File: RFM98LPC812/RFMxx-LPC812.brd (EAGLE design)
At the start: 60 x 38.7 mm, 33 parts, among them X1 BU-SMA-V, X2 BU-SMA-V

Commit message: getting close to done
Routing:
- net N$14: track 19.0 -> 6.93 mm
- net GND: track 214.8 -> 225.6 mm, vias 2 -> 3
- net VCC: track 119.8 -> 113.9 mm
- net N$45: track 0.00 -> 3.30 mm
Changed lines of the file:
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@@
 <description language="de">&lt;b&gt;EAGLE Design Rules&lt;/b&gt;
 &lt;p&gt;
-Die Standard-Design-Rules sind so gewÃ¤hlt, dass sie fÃ¼r
+Die Standard-Design-Rules sind so gewÃÂ¤hlt, dass sie fÃÂ¼r
 die meisten Anwendungen passen. Sollte ihre Platine
 besondere Anforderungen haben, treffen Sie die erforderlichen
@@
 <contactref element="C2" pad="1"/>
 <contactref element="JP8" pad="1"/>
-<wire x1="18.5166" y1="26.5176" x2="20.8026" y2="26.5176" width="0.254" layer="1"/>
-<wire x1="20.8026" y1="26.5176" x2="20.955" y2="26.455" width="0.254" layer="1"/>
-<wire x1="18.5166" y1="26.5176" x2="18.3642" y2="26.67" width="0.254" layer="1"/>
 <wire x1="39.0906" y1="12.7508" x2="39.140371875" y2="12.584065625" width="0.254" layer="16"/>
 <wire x1="10.795" y1="36.195" x2="10.795" y2="37.7825" width="0.4064" layer="1"/>
@@
 <wire x1="56.9214" y1="35.2044" x2="56.99" y2="35.21" width="0.254" layer="1"/>
 <wire x1="56.9214" y1="35.2044" x2="56.8325" y2="35.2425" width="0.254" layer="1"/>
-<wire x1="10.795" y1="36.195" x2="10.795" y2="26.67" width="0.4064" layer="1"/>
-<wire x1="10.795" y1="26.67" x2="16.9164" y2="26.67" width="0.4064" layer="1"/>
-<wire x1="16.9164" y1="26.67" x2="18.288" y2="26.67" width="0.4064" layer="1"/>
-<wire x1="18.288" y1="26.67" x2="18.3642" y2="26.67" width="0.4064" layer="1"/>
-<wire x1="18.3642" y1="26.67" x2="18.415" y2="26.67" width="0.4064" layer="1"/>
-<wire x1="18.288" y1="26.7462" x2="18.3642" y2="26.67" width="0.254" layer="1"/>
-<wire x1="18.288" y1="26.7462" x2="18.288" y2="26.67" width="0.254" layer="1"/>
-<wire x1="16.9164" y1="21.0312" x2="16.9164" y2="26.67" width="0.254" layer="1"/>
 <wire x1="52.578" y1="15.9512" x2="52.705" y2="15.875" width="0.254" layer="1"/>
 <wire x1="48.4632" y1="10.4648" x2="48.006" y2="10.4648" width="0.254" layer="1"/>
@@
 <wire x1="48.006" y1="10.4648" x2="47.85" y2="10.255" width="0.254" layer="1"/>
 <wire x1="52.578" y1="15.7226" x2="52.705" y2="15.875" width="0.254" layer="1"/>
-<wire x1="18.3642" y1="8.89" x2="16.9164" y2="21.0312" width="0" layer="19" extent="1-1"/>
+<wire x1="18.3642" y1="26.67" x2="20.955" y2="26.455" width="0" layer="19" extent="1-1"/>
+<wire x1="10.795" y1="36.195" x2="18.3642" y2="26.67" width="0" layer="19" extent="1-1"/>
+<wire x1="24.765" y1="9.525" x2="20.955" y2="26.455" width="0" layer="19" extent="1-16"/>
+<wire x1="10.795" y1="36.195" x2="10.795" y2="26.67" width="0.4064" layer="1"/>
+<wire x1="20.955" y1="26.67" x2="18.415" y2="26.67" width="0.6096" layer="1"/>
+<wire x1="10.795" y1="26.67" x2="18.415" y2="26.67" width="0.4064" layer="1"/>
 </signal>
 <signal name="N$6">
@@
 <wire x1="24.4602" y1="23.3172" x2="24.003" y2="22.86" width="0.254" layer="1"/>
 <wire x1="24.4602" y1="23.3172" x2="24.61" y2="23.495" width="0.254" layer="1"/>
-<wire x1="24.6888" y1="23.3172" x2="36.8046" y2="23.3172" width="0.254" layer="1"/>
+<wire x1="24.6888" y1="23.3172" x2="36.8046" y2="23.3172" width="0" layer="19" extent="1-16"/>
 <wire x1="36.8046" y1="23.3172" x2="36.99" y2="23.21" width="0.254" layer="1"/>
 <wire x1="24.6888" y1="23.3172" x2="24.61" y2="23.495" width="0.254" layer="1"/>
@@
 <contactref element="C2" pad="2"/>
 <contactref element="U$1" pad="16"/>
-<wire x1="18.5166" y1="28.1178" x2="20.8026" y2="28.1178" width="0.254" layer="1"/>
+<wire x1="18.5166" y1="28.1178" x2="20.8026" y2="28.1178" width="0.6096" layer="1"/>
 <wire x1="20.8026" y1="28.1178" x2="20.955" y2="28.155" width="0.254" layer="1"/>
 <wire x1="18.5166" y1="28.1178" x2="18.3642" y2="27.94" width="0.254" layer="1"/>
 <wire x1="18.288" y1="27.8892" x2="18.3642" y2="27.94" width="0.254" layer="1"/>
 <contactref element="R1" pad="1"/>
-<wire x1="33.8328" y1="30.6324" x2="33.6674" y2="30.4701" width="0.254" layer="16"/>
-<wire x1="33.8328" y1="35.433" x2="33.6674" y2="35.5699" width="0.254" layer="16"/>
 <wire x1="58.0644" y1="8.4074" x2="58.0644" y2="10.6934" width="0.254" layer="1"/>
 <wire x1="57.3786" y1="7.7216" x2="58.0644" y2="8.4074" width="0.254" layer="1"/>
@@
 <wire x1="1.8288" y1="36.1188" x2="1.69" y2="36.195" width="0.254" layer="1"/>
 <via x="6.6294" y="34.9758" extent="1-16" drill="0.6096"/>
+<wire x1="13.335" y1="20.955" x2="16.6878" y2="20.955" width="0" layer="19" extent="1-16"/>
 <wire x1="13.335" y1="20.955" x2="20.955" y2="20.955" width="0.4064" layer="16"/>
 <wire x1="20.955" y1="20.955" x2="20.955" y2="22.225" width="0.254" layer="16"/>
@@
 <wire x1="55.245" y1="7.62" x2="57.15" y2="7.62" width="0.4064" layer="16"/>
 <wire x1="57.15" y1="7.62" x2="57.15" y2="2.54" width="0.4064" layer="16"/>
-<wire x1="57.15" y1="2.54" x2="50.165" y2="2.54" width="0.4064" layer="16"/>
-<wire x1="50.165" y1="2.54" x2="50.165" y2="1.27" width="0.4064" layer="16"/>
-<wire x1="50.165" y1="1.27" x2="15.24" y2="1.27" width="0.4064" layer="16"/>
+<wire x1="57.15" y1="2.54" x2="52.1208" y2="2.54" width="0.4064" layer="16"/>
+<wire x1="52.1208" y1="2.54" x2="52.07" y2="2.54" width="0.4064" layer="16"/>
+<wire x1="52.07" y1="2.54" x2="52.07" y2="1.27" width="0.4064" layer="16"/>
+<wire x1="52.07" y1="1.27" x2="15.24" y2="1.27" width="0.4064" layer="16"/>
 <wire x1="15.24" y1="1.27" x2="1.905" y2="1.27" width="0.4064" layer="16"/>
 <wire x1="1.905" y1="2.54" x2="1.905" y2="3.175" width="0.4064" layer="16"/>
@@
 <contactref element="R4" pad="2"/>
 <wire x1="15.24" y1="1.27" x2="15.24" y2="10.16" width="0.4064" layer="16"/>
-<wire x1="34.29" y1="31.0896" x2="33.8328" y2="35.433" width="0" layer="19" extent="1-16"/>
-<wire x1="28.36" y1="21.9075" x2="26.67" y2="22.225" width="0" layer="19" extent="1-16"/>
-<wire x1="15.24" y1="10.16" x2="13.335" y2="20.955" width="0" layer="19" extent="16-16"/>
-<wire x1="57.1599" y1="2.5301" x2="57.15" y2="2.54" width="0" layer="19" extent="16-16"/>
-<wire x1="57.1599" y1="7.6299" x2="57.15" y2="7.62" width="0" layer="19" extent="16-16"/>
-<wire x1="4.445" y1="1.69" x2="4.3434" y2="1.778" width="0" layer="19" extent="1-1"/>
+<wire x1="33.8328" y1="30.6324" x2="33.8328" y2="35.433" width="0.254" layer="16"/>
+<wire x1="33.8328" y1="35.433" x2="33.6674" y2="35.5699" width="0.254" layer="16"/>
+<wire x1="33.8328" y1="30.6324" x2="33.6674" y2="30.4701" width="0.254" layer="16"/>
+<wire x1="4.3434" y1="1.8288" x2="4.445" y2="1.69" width="0.254" layer="1"/>
+<wire x1="4.3434" y1="1.8288" x2="4.3434" y2="1.778" width="0.254" layer="1"/>
+<wire x1="52.1208" y1="2.5146" x2="52.1208" y2="2.54" width="0.254" layer="16"/>
+<wire x1="52.1208" y1="2.5146" x2="52.0601" y2="2.5301" width="0.254" layer="16"/>
+<wire x1="16.6878" y1="11.6586" x2="16.6878" y2="20.955" width="0" layer="19" extent="1-16"/>
+<wire x1="15.3162" y1="10.287" x2="16.6878" y2="11.6586" width="0" layer="19" extent="1-16"/>
+<wire x1="15.3162" y1="10.287" x2="15.24" y2="10.16" width="0.254" layer="16"/>
+<wire x1="57.15" y1="7.7724" x2="57.1599" y2="7.6299" width="0.254" layer="16"/>
+<wire x1="57.15" y1="7.7724" x2="57.15" y2="7.62" width="0.254" layer="16"/>
+<wire x1="28.36" y1="21.9075" x2="26.67" y2="21.9075" width="0.4064" layer="1"/>
+<wire x1="26.67" y1="21.9075" x2="26.67" y2="22.225" width="0.4064" layer="1"/>
+<wire x1="26.67" y1="22.225" x2="26.67" y2="22.225" width="0" layer="19" extent="1-16"/>
+<via x="15.24" y="10.16" extent="1-16" drill="0.6"/>
+<wire x1="15.24" y1="10.16" x2="18.415" y2="10.16" width="0.4064" layer="1"/>
 </signal>
 <signal name="N$11">
@@
 <contactref element="C1" pad="2"/>
 <contactref element="U$5" pad="16"/>
-<wire x1="18.3642" y1="10.16" x2="21.59" y2="10.375" width="0" layer="19" extent="1-1"/>
+<wire x1="18.5166" y1="10.287" x2="21.4884" y2="10.287" width="0.6096" layer="1"/>
+<wire x1="21.4884" y1="10.287" x2="21.59" y2="10.375" width="0.254" layer="1"/>
+<wire x1="18.5166" y1="10.287" x2="18.3642" y2="10.16" width="0.254" layer="1"/>
 </signal>
 </signals>

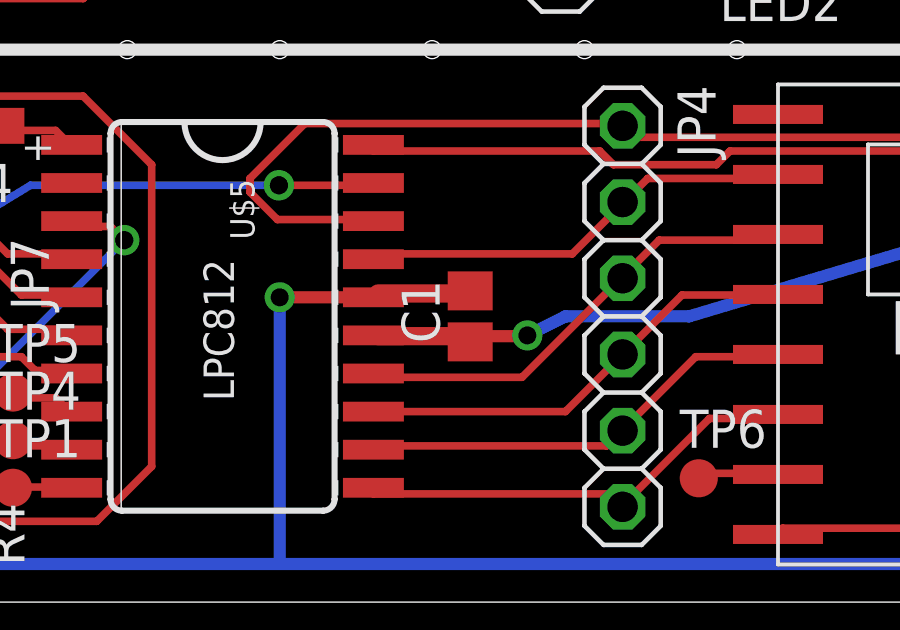
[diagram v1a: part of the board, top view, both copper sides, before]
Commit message: fixed inconsistency by hand editing .brd XML
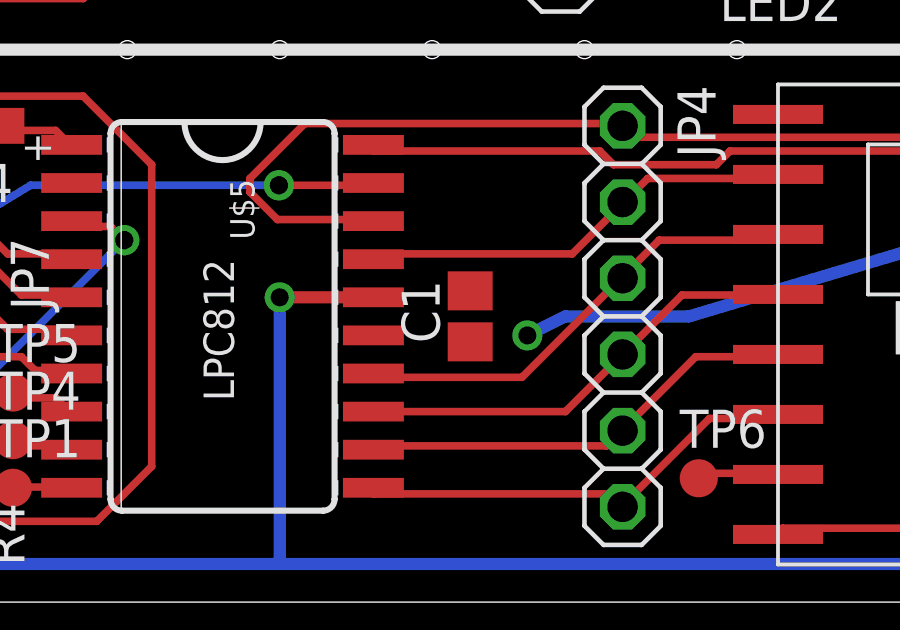
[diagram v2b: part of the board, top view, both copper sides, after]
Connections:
- removed net N$45: C1.2, U$5.16
- net VCC: no longer C1.1, U$5.15
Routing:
- net VCC: track 113.9 -> 108.5 mm
- net N$45: track 3.30 -> 0.00 mm
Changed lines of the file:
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@@
 <contactref element="U$2" pad="VCC"/>
 <contactref element="JP5" pad="1"/>
-<contactref element="C1" pad="1"/>
-<contactref element="U$5" pad="15"/>
 <wire x1="52.705" y1="15.875" x2="50.165" y2="15.875" width="0.4064" layer="16"/>
 <wire x1="50.165" y1="15.875" x2="39.140371875" y2="12.584065625" width="0.4064" layer="16"/>
@@
 <wire x1="24.765" y1="9.525" x2="23.495" y2="8.89" width="0.4064" layer="16"/>
 <via x="23.495" y="8.89" extent="1-16" drill="0.6"/>
-<wire x1="23.3172" y1="8.8646" x2="21.717" y2="8.8646" width="0.4064" layer="1"/>
-<wire x1="21.717" y1="8.8646" x2="21.59" y2="8.675" width="0.254" layer="1"/>
-<wire x1="23.3172" y1="8.8646" x2="23.495" y2="8.89" width="0.254" layer="1"/>
-<wire x1="21.4884" y1="8.8646" x2="18.5166" y2="8.8646" width="0.6096" layer="1"/>
-<wire x1="18.5166" y1="8.8646" x2="18.3642" y2="8.89" width="0.254" layer="1"/>
-<wire x1="21.4884" y1="8.8646" x2="21.59" y2="8.675" width="0.254" layer="1"/>
 <contactref element="U$3" pad="VCC"/>
 <contactref element="U$1" pad="15"/>
@@
 <wire x1="8.2296" y1="21.4884" x2="8.3058" y2="21.59" width="0.254" layer="1"/>
 </signal>
-<signal name="N$45">
-<contactref element="C1" pad="2"/>
-<contactref element="U$5" pad="16"/>
-<wire x1="18.5166" y1="10.287" x2="21.4884" y2="10.287" width="0.6096" layer="1"/>
-<wire x1="21.4884" y1="10.287" x2="21.59" y2="10.375" width="0.254" layer="1"/>
-<wire x1="18.5166" y1="10.287" x2="18.3642" y2="10.16" width="0.254" layer="1"/>
-</signal>
 </signals>

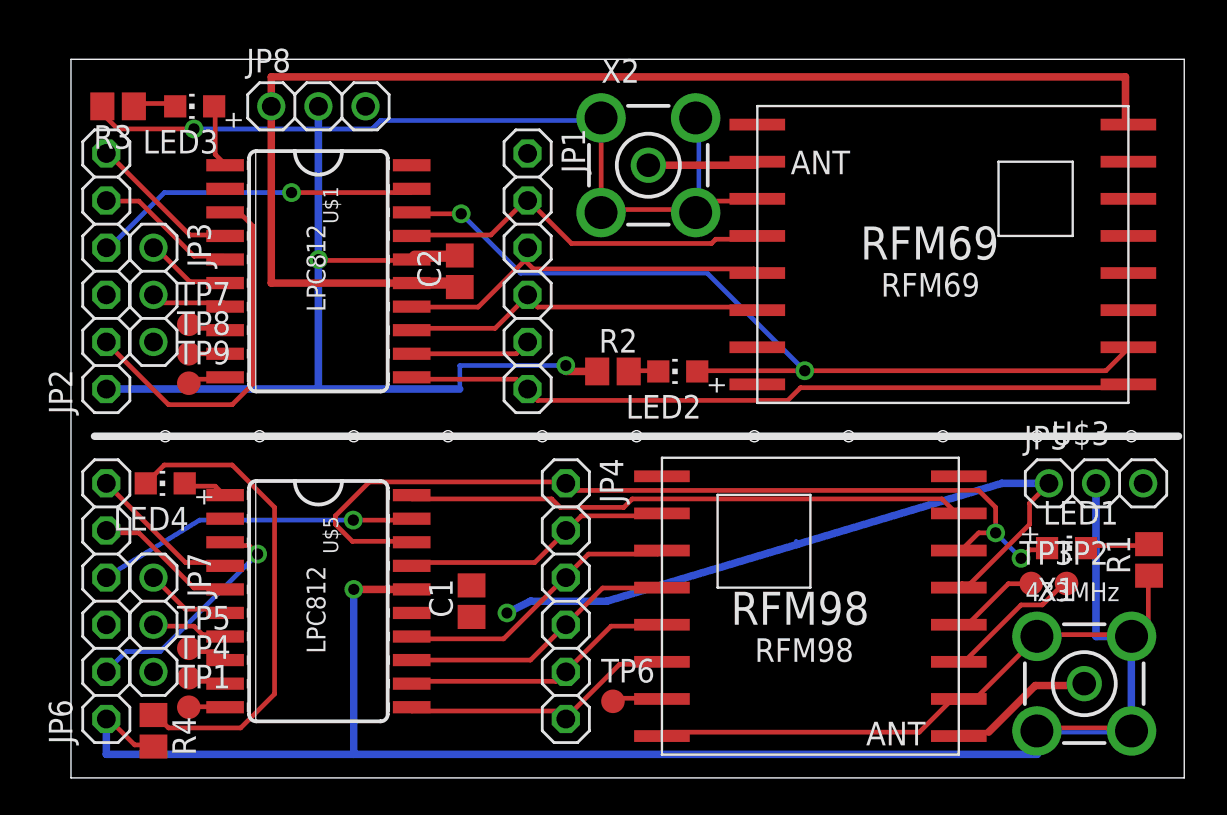
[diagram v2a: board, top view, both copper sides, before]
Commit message: added TPs for DIO0..5 on RFM69 side
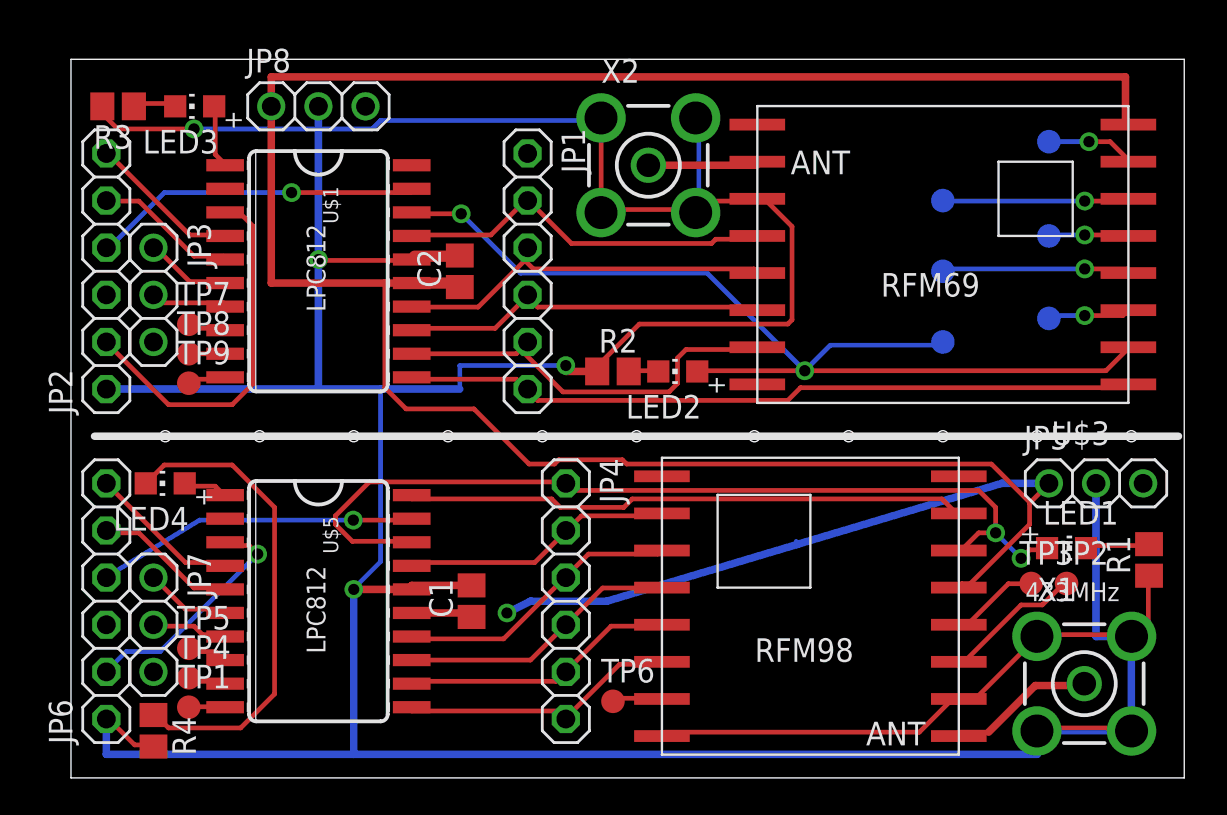
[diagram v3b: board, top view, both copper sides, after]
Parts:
- added DIO0, DIO1, DIO2, DIO3, DIO4, DIO5: TPB1,27, testpad:B1,27
- C1: value 0.1uF -> 100nF
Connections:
- new net N$45: C1.2, U$5.16
- new net N$46: C1.1, U$5.15
- new net N$47: DIO1.TP, U$3.DIO1
- new net N$48: DIO2.TP, U$3.DIO2
- new net N$49: DIO3.TP, U$3.DIO3
- new net N$50: DIO4.TP, U$3.DIO4
- new net N$51: DIO5.TP, U$3.DIO5
- net N$24: now also DIO0.TP
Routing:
- net VCC: track 108.5 -> 152.1 mm
- net GND: track 225.6 -> 256.3 mm
- net N$14: track 6.93 -> 23.0 mm
- net N$48: track 0.00 -> 10.2 mm, vias 0 -> 1
- net N$50: track 0.00 -> 10.1 mm, vias 0 -> 1
- net N$24: track 48.5 -> 56.6 mm
- net N$51: track 0.00 -> 4.77 mm, vias 0 -> 1
- net N$47: track 0.00 -> 4.49 mm, vias 0 -> 1
- net N$49: track 0.00 -> 4.31 mm, vias 0 -> 1
- net N$46: track 0.00 -> 3.44 mm
- net N$45: track 0.00 -> 3.44 mm
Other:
- board text removed: "RFM69"
- board text removed: "RFM98"
